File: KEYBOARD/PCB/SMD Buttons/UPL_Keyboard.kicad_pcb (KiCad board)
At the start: 2 copper layers, 320 x 153 mm, 49 parts, among them J1 Conn_02x13_Odd_Even, SW1 START, SW10 8, SW11 9, SW12 SELECT, SW13 HELP, SW14 TABRIGHT, SW15 4, SW16 5, SW17 6, SW18 BACKSP, SW19 TABLEFT, SW2 SINGLE, SW20 PGUP, SW21 1, SW22 2, SW23 3, SW24 CANCEL, SW25 PGDOWN, SW26 0, SW27 POINT, SW28 MINUS, SW29 ENTER, SW3 STOP, SW30 LEFT, SW31 RIGHT, SW32 UP, SW33 DOWN, SW34 F1, SW35 F2, SW36 F3, SW37 F4, SW38 F5, SW39 F6, SW4 HCOPY, SW40 F7, SW41 F8, SW5 SYSTEM, SW6 CONTRAST, SW7 OUTPUT, SW8 LOCAL, SW9 7

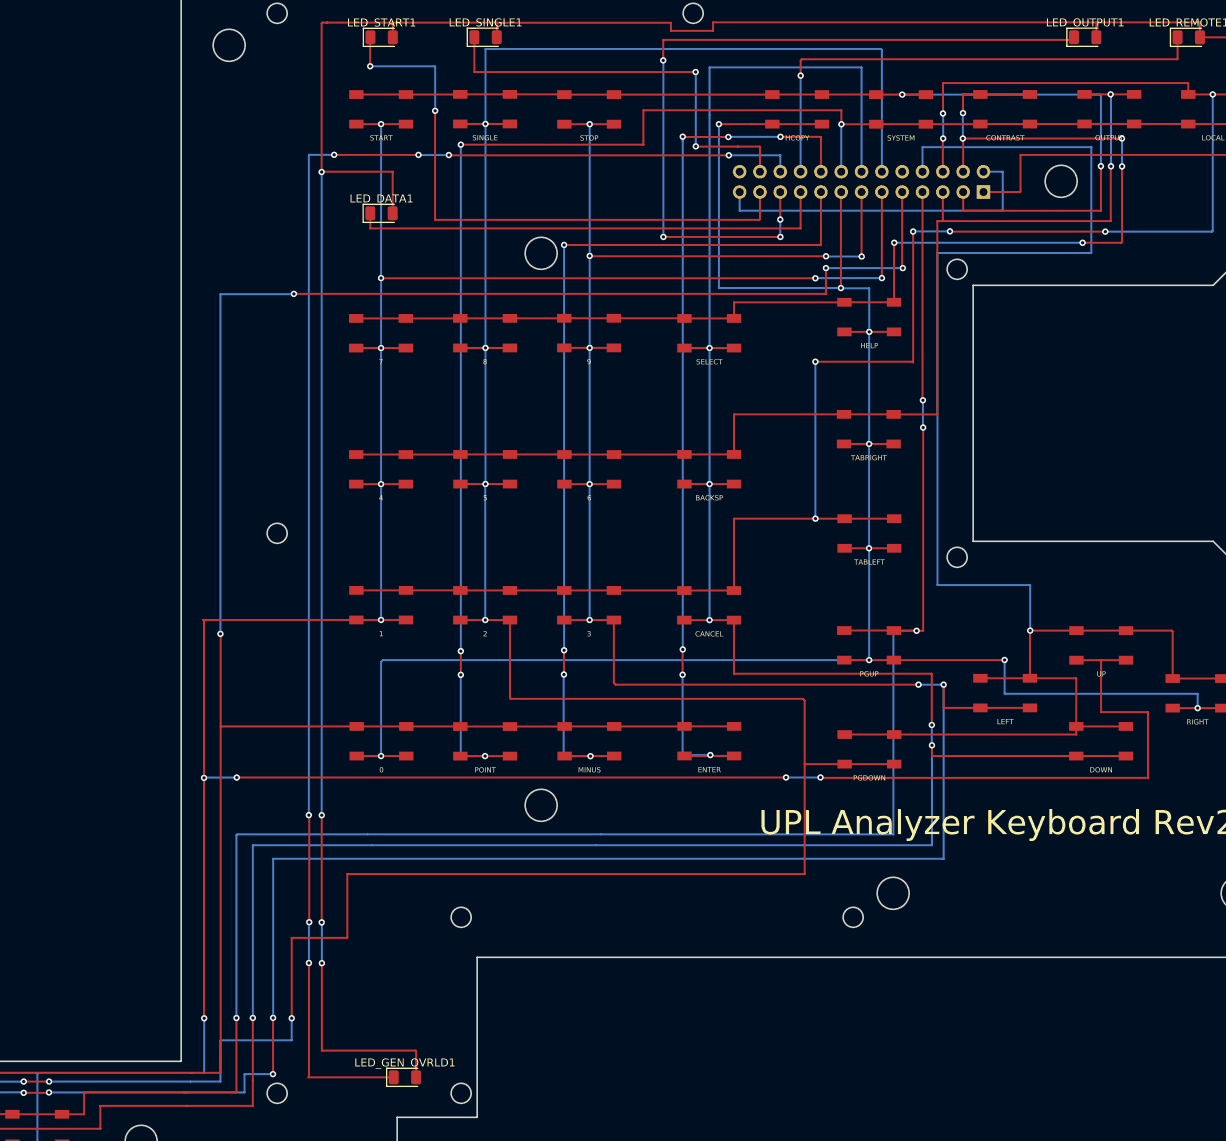
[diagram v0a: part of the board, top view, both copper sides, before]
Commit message: cleanup pcb
cleanup move connector for more clearance screw
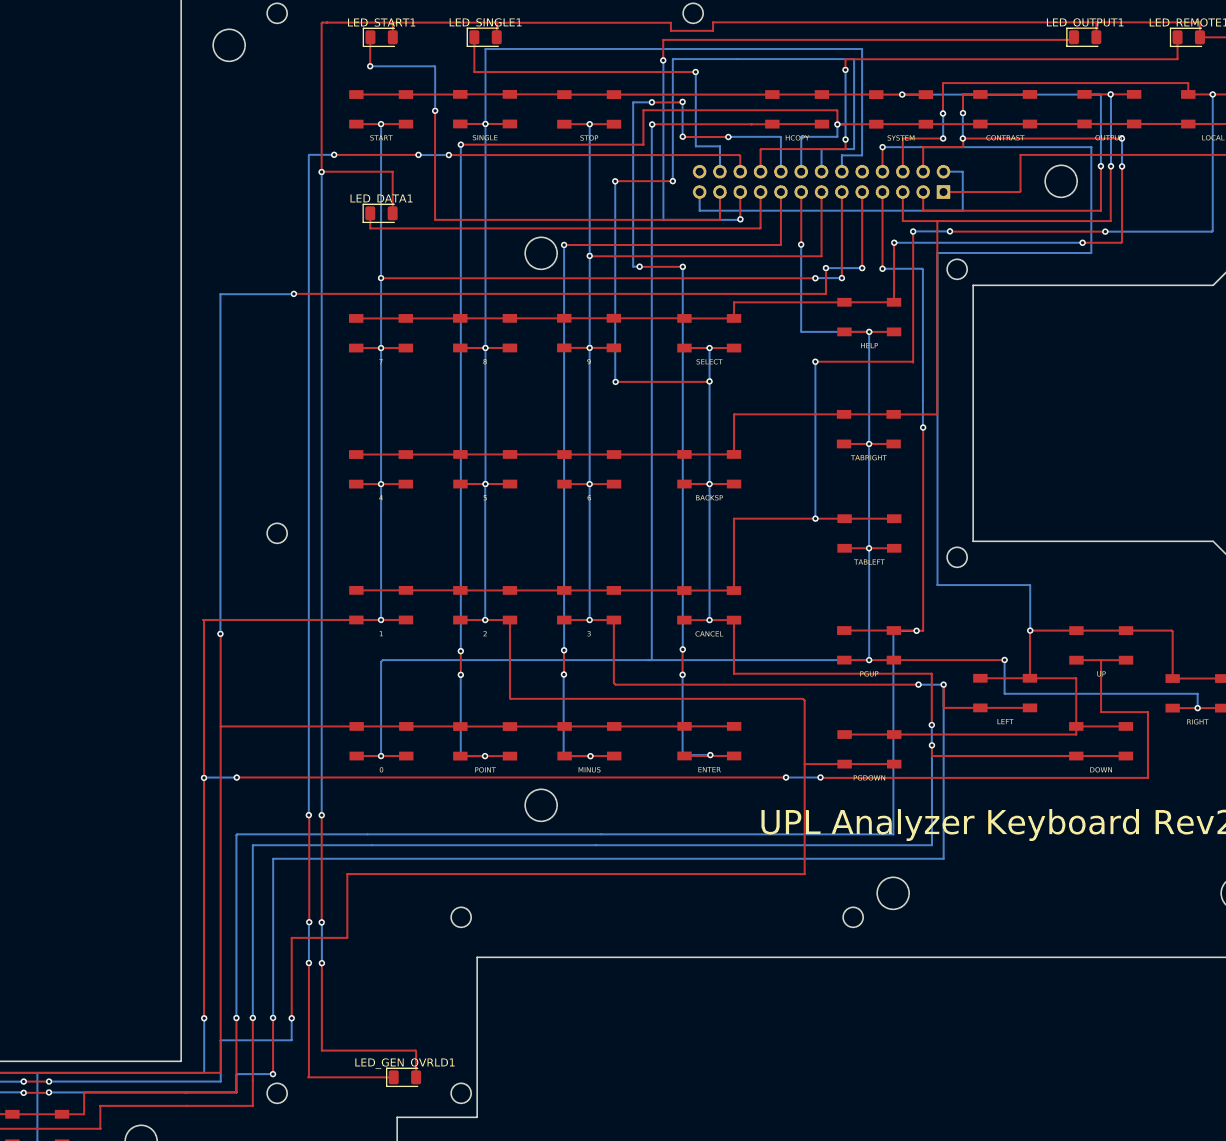
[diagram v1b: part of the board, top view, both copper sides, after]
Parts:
- moved J1 5.00 mm to (315.4, 99.7)
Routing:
- net BTN_COL_5: track 264.7 -> 309.8 mm
- net BTN_COL_4: track 430.6 -> 463.6 mm, vias 6 -> 10
- net BTN_COL_8: track 108.8 -> 124.2 mm, vias 6 -> 9
- net LED_OUTPUT: track 96.4 -> 87.1 mm, vias 4 -> 2
- net BTN_ROW_6: track 205.5 -> 210.7 mm, vias 1 -> 2
- net BTN_COL_3: track 481.4 -> 476.3 mm, vias 17 -> 15
- net BTN_ROW_7: track 430.9 -> 425.7 mm
- net BTN_COL_6: track 194.8 -> 199.9 mm
- net BTN_ROW_2: track 156.3 -> 161.4 mm
- net BTN_ROW_4: track 229.2 -> 234.2 mm
- net LED_DATA: track 60.2 -> 55.2 mm
- net LED_GEN_OVRLD: track 187.1 -> 182.0 mm, vias 7 -> 6
- net BTN_ROW_1: track 130.1 -> 135.1 mm
- net LED_REMOTE: track 63.8 -> 68.8 mm, vias 1 -> 2
- net BTN_COL_7: track 112.4 -> 107.4 mm
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
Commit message: Update of SMD button manufacturer
Change SMD buttons to EVQQ2P02W
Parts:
- SW1, SW10, SW11, SW12, SW13, SW14, SW15, SW16, SW17, SW18, SW19, SW2, SW20, SW21, SW22, SW23, SW24, SW25, SW26, SW27, SW28, SW29, SW3, SW30, SW31, SW32, SW33, SW34, SW35, SW36, SW37, SW38, SW39, SW4, SW40, SW41, SW5, SW6, SW7, SW8, SW9: footprint BVKSound:SW_SKQGAFE010 -> BVKSound:EVQ-Q2B01W

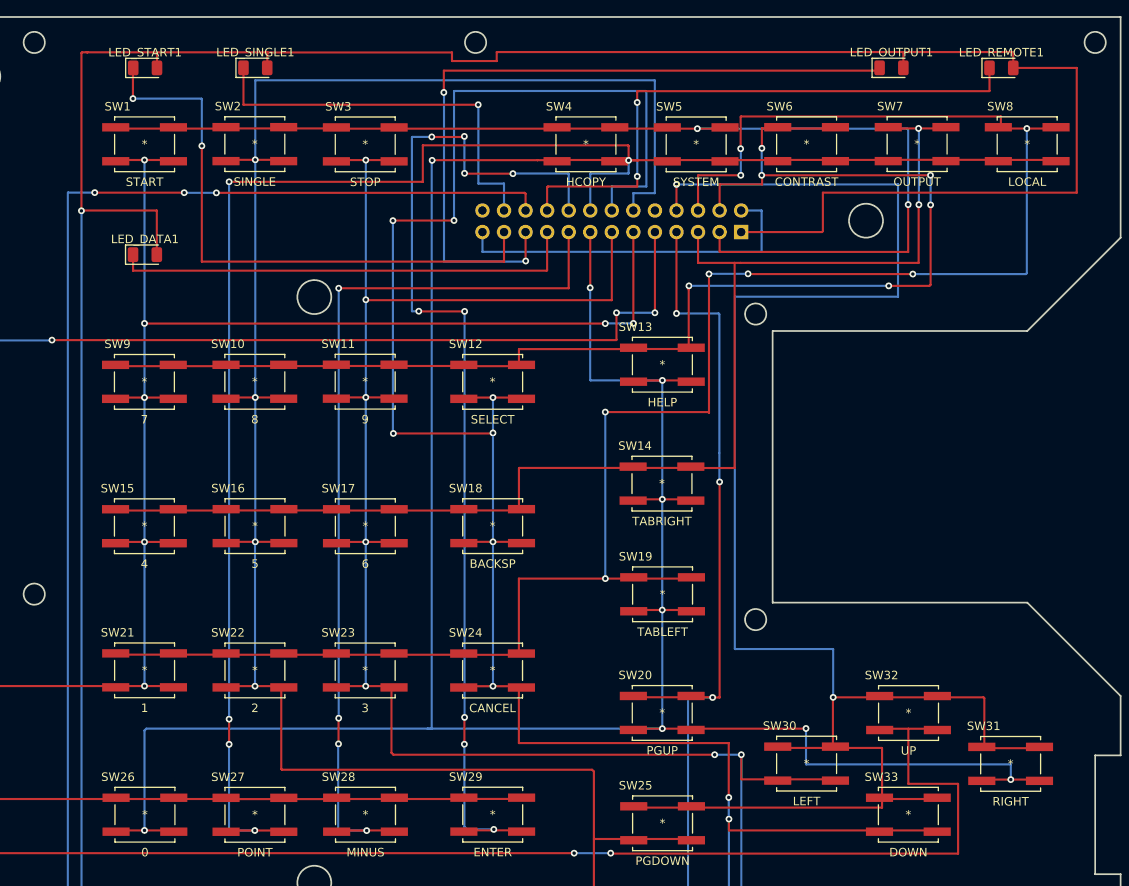
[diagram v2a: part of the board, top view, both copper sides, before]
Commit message: Finalized design with FFC Connector
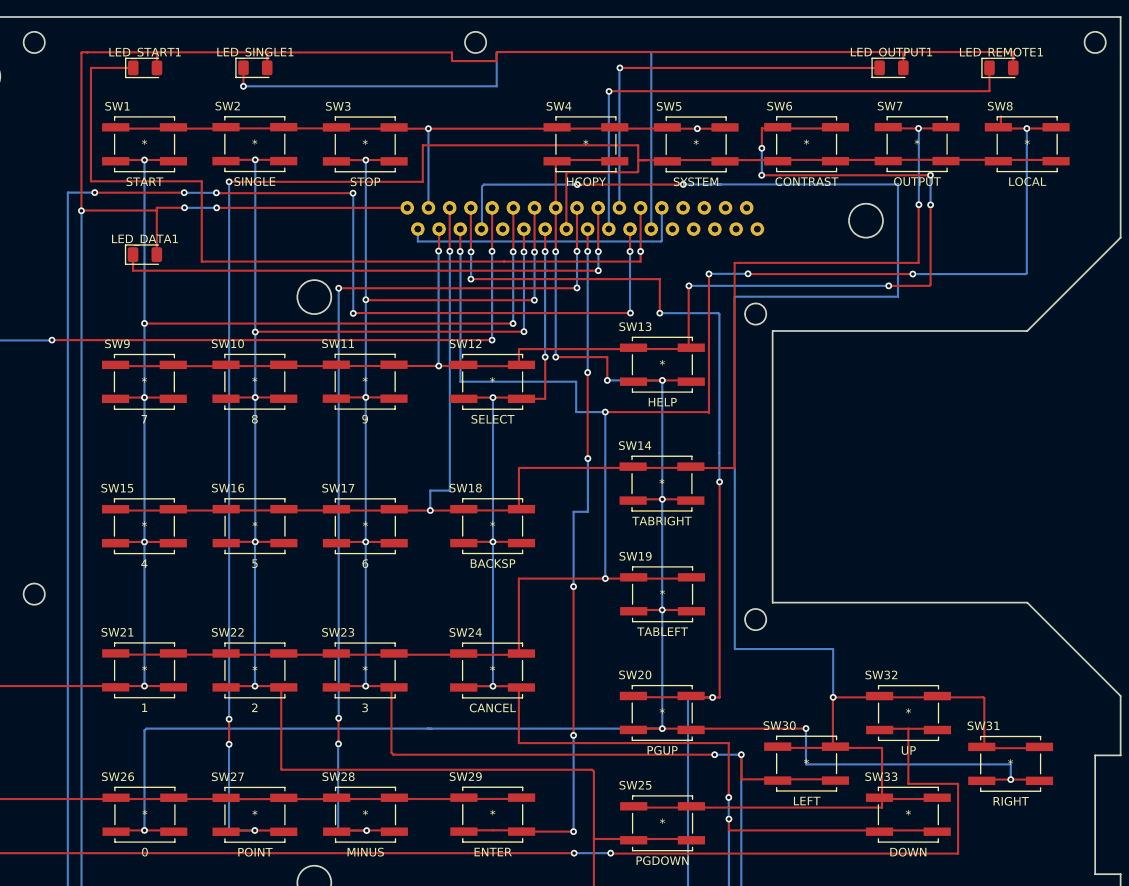
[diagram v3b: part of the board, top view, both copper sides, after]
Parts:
- J1: footprint Connector_PinHeader_2.54mm:PinHeader_2x13_P2.54mm_Vertical -> BVKSound:0520443445_Mirrored
- moved J1 18.8 mm to (296.7, 98.1), turned to 180 degrees
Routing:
- net BTN_COL_4: track 463.6 -> 386.3 mm, vias 10 -> 8
- net BTN_COL_5: track 309.8 -> 240.3 mm, vias 9 -> 10
- net BTN_ROW_1: track 135.1 -> 80.5 mm
- net LED_OUTPUT: track 87.1 -> 47.1 mm, vias 2 -> 1
- net BTN_COL_8: track 124.2 -> 85.1 mm, vias 9 -> 6
- net LED_A: track 343.3 -> 306.9 mm, vias 4 -> 6
- net LED_GEN_OVRLD: track 182.0 -> 216.5 mm, vias 6 -> 10
- net BTN_COL_2: track 510.6 -> 480.0 mm, vias 9 -> 12
- net BTN_ROW_3: track 153.5 -> 183.5 mm, vias 2 -> 4
- net LED_START: track 70.0 -> 98.9 mm, vias 2 -> 1
- net LED_SINGLE: track 47.5 -> 75.0 mm
- net BTN_ROW_5: track 303.6 -> 330.8 mm, vias 4 -> 6
- net BTN_ROW_6: track 210.7 -> 235.7 mm, vias 2 -> 3
- net BTN_ROW_7: track 425.7 -> 409.4 mm
- net BTN_COL_1: track 566.8 -> 555.5 mm
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
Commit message: final update rev3
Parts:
- moved J1 2.73 mm to (296.7, 95.4)
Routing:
- net BTN_ROW_6: track 235.7 -> 251.7 mm
- net LED_A: track 306.9 -> 309.9 mm
- net BTN_COL_6: track 206.4 -> 203.6 mm
- net BTN_ROW_5: track 330.8 -> 333.5 mm
- net BTN_COL_4: track 386.3 -> 389.1 mm
- net BTN_COL_3: track 470.0 -> 472.8 mm
- net BTN_COL_1: track 555.5 -> 558.2 mm
- net LED_GEN_OVRLD: track 216.5 -> 219.2 mm
- net BTN_ROW_4: track 226.1 -> 228.8 mm
- net BTN_ROW_3: track 183.5 -> 186.3 mm
- net BTN_COL_7: track 111.2 -> 113.9 mm
- net LED_START: track 98.9 -> 101.7 mm
- net LED_DATA: track 64.1 -> 66.9 mm
- net BTN_ROW_2: track 168.5 -> 171.2 mm
- net BTN_COL_2: track 480.0 -> 482.8 mm
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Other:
- board text added: "UPL Analyzer Keyboard Rev3"
- board text added: "UPL Analyzer Keyboard Rev3 03/2021"
- board text removed: "UPL Analyzer Keyboard Rev2"
- board text removed: "UPL Analyzer Keyboard Rev2 02/2021"
